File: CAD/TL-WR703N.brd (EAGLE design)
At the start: 47.4 x 50 mm, 241 parts, among them T1 H1601CG, U1 AR9331-AL1A, U2 A3S56F40FTP

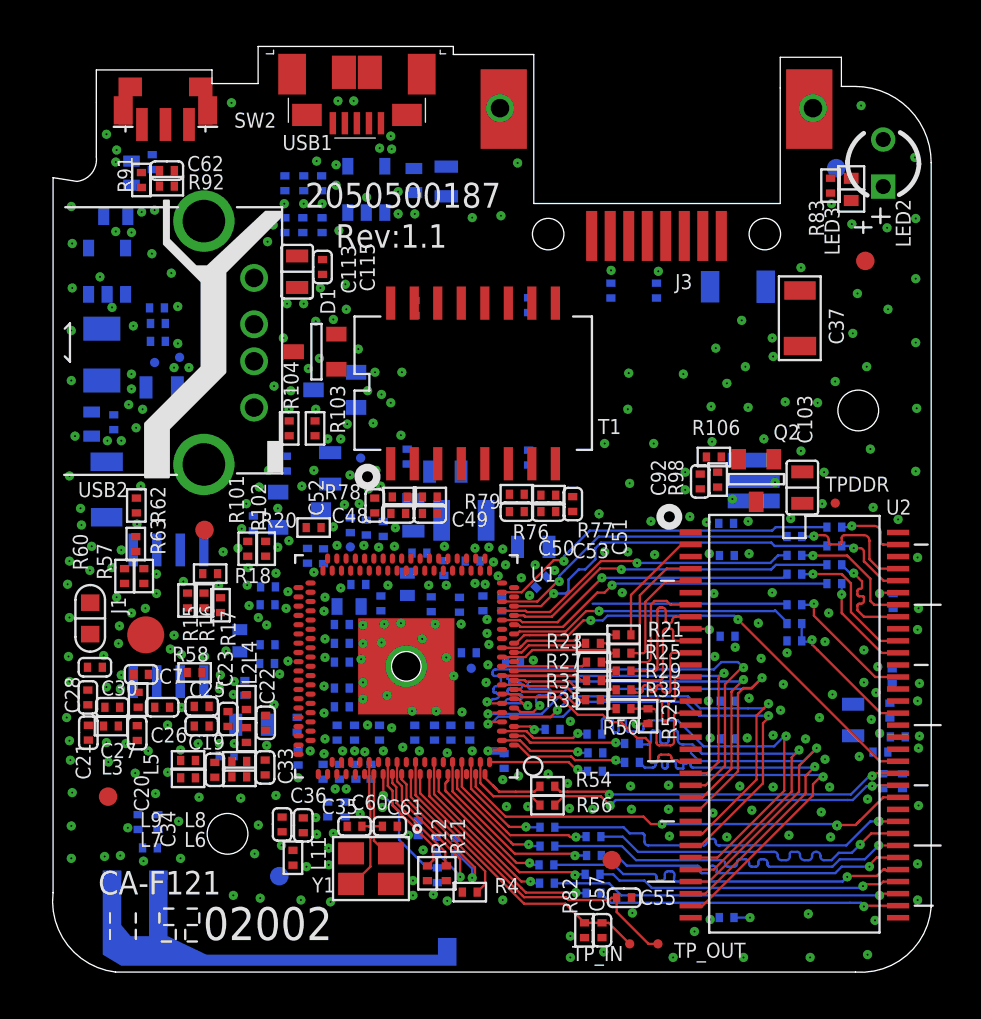
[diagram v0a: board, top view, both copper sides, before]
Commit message: Almost completed traces on top side
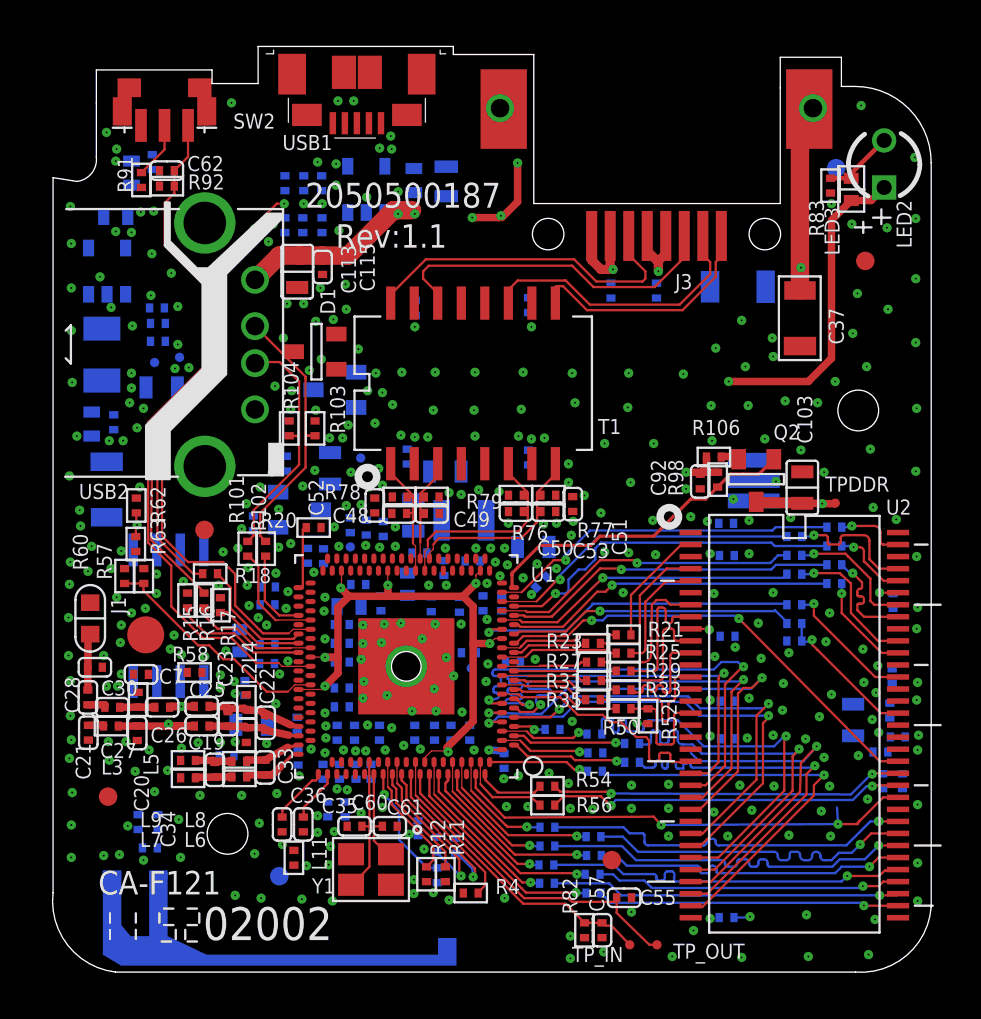
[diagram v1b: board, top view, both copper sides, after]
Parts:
- moved USB2 0.11 mm to (-1.22, 34.4)
- moved C49 0.10 mm to (21.3, 25.3)
- moved R79 0.10 mm to (21.3, 26.2)
- moved R76 0.07 mm to (25.9, 26.3)
- moved LED2 0.07 mm to (45.7, 44.1)
- moved R11 0.07 mm to (22.0, 5.79)
- moved R12 0.07 mm to (21.0, 5.79)
- moved R4 0.07 mm to (23.4, 4.78)
- moved TP_OUT 0.07 mm to (33.5, 1.98)
- moved SW2 0.07 mm to (6.88, 46.2)
- moved C48 0.05 mm to (19.6, 25.3)
- moved C50 0.05 mm to (25.9, 25.4)
- moved TP_IN 0.05 mm to (32.0, 1.98)
- renumbered E$8 to GND
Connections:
- removed net S$41: R37.1, U1.B14
- new net S$102: R101.2, U1.B43
- new net S$103: U1.A58, U1.B13, U1.B21, U1.B31, U1.B36, U1.B47, U1.B69
- new net S$104: D1.3, R102.1, R103.1, USB2.2
- new net S$105: C62.2, R92.2, SW2.3, U1.B48
- new net S$106: R91.2, SW2.2
- new net S$107: SW2.S$1, SW2.S$2
- new net S$108: J3.S$1, USB1.S$1, USB1.S$2, USB1.S$3, USB1.S$4, USB1.S$5, USB1.S$6, USB2.S$1
- new net S$109: R15.2, U1.A54
- new net S$110: R16.2, U1.B46
- new net S$111: R16.1
- new net S$113: R18.1
- new net S$158: C25.1, C26.2
- new net S$168: C19.1, C20.2, L3.2
- new net S$263: U1.B44
- new net S$269: C113.2, C115.2, USB2.1
- new net S$29: J3.8, T1.9
- new net S$290: J3.1, J3.2
- new net S$291: J3.4, J3.5
- new net S$292: C37.2, J3.S$2
- new net S$321: LED2.A, LED3.A
- new net S$329: C92.2, R106.2, R98.2
- new net S$354: C36.2, U1.A68
- new net S$357: C35.2, U1.A69
- new net S$359: C103.1, Q2.3, TPDDR.1
- new net S$365: J3.6, T1.14
- new net S$367: J3.3, T1.16
- new net S$370: C49.1, R79.1, T1.3, U1.A32
- new net S$371: C48.2, R78.2, T1.1, U1.B28
- new net S$372: C52.2, R78.1
- new net S$373: C53.1, R77.1, T1.8, U1.A31
- new net S$374: C50.2, R76.2, T1.6, U1.B27
- new net S$379: Q2.1, R98.1, U1.A20
- new net S$380: Q2.2, R106.1
- new net S$42: J3.7, T1.11
- new net S$420: R37.1, U1.B14
- new net S$452: R62.2, R63.1
- new net S$50: C33.2, L8.1, U1.A64
- new net S$55: LED2.K, LED3.C, R83.2
- new net S$68: C33.1, L6.1, U1.A65
- new net S$70: C34.2, L8.2, L9.1
- new net S$73: C34.1, L6.2, L7.1
- new net S$75: C19.2, C22.1, C23.1, L2.2, U1.A63
- new net S$78: C22.2, C23.2, C25.2, L4.1, U1.A62
- new net S$79: R57.2, R60.2, U1.B50
- new net S$80: C21.2, L3.1
- new net S$81: C27.1, C28.1
- new net S$85: R101.1, R104.1, USB2.3
- new net S$87: C28.2, C30.1, J1.1
- new net S$94: C26.1, C27.2, L5.1
- new net S$95: R20.1, U1.A47
- new net S$96: R17.2, U1.A53
- new net S$97: R18.2, U1.A52
- new net S$98: R102.2, U1.A50
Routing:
- net S$105: track 0.00 -> 38.0 mm
- net S$103: track 0.00 -> 32.6 mm, vias 0 -> 7
- net S$263: track 0.00 -> 30.6 mm
- net S$113: track 0.00 -> 24.4 mm
- net S$111: track 0.00 -> 23.3 mm
- net S$365: track 0.00 -> 18.6 mm
- net S$367: track 0.00 -> 18.2 mm
- net S$420: track 0.00 -> 17.8 mm
- net S$379: track 0.00 -> 17.5 mm
- net S$321: track 0.00 -> 17.1 mm
- net S$104: track 0.00 -> 15.5 mm
- net S$42: track 0.00 -> 15.3 mm
- net S$85: track 0.00 -> 13.7 mm, vias 1 -> 0
- net S$29: track 0.00 -> 13.2 mm
- net S$79: track 0.00 -> 12.9 mm, vias 1 -> 0
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
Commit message: Definitely good progress on top side!
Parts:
- moved LED2 0.11 mm to (45.7, 44.2)
- moved R102 0.11 mm to (12.4, 23.5)
- moved C113 0.11 mm to (14.1, 38.4)
- moved USB1 0.11 mm to (17.2, 48.9)
- moved C48 0.10 mm to (19.6, 25.4)
- moved C49 0.10 mm to (21.3, 25.4)
- moved R101 0.10 mm to (11.4, 23.5)
- moved R17 0.10 mm to (9.91, 20.4)
- moved R52 0.10 mm to (32.9, 14.3)
- moved R63 0.10 mm to (5.33, 23.7)
- moved C52 0.10 mm to (18.2, 25.8)
- moved C92 0.10 mm to (35.8, 27.1)
- moved R15 0.10 mm to (8.13, 20.7)
- moved R16 0.10 mm to (9.02, 20.7)
- moved R20 0.07 mm to (14.9, 24.6)
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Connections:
- net S$452 renamed S$159
- removed net S$321: LED2.A, LED3.A
- removed net S$357: C35.2, U1.A69
- removed net S$367: J3.3, T1.16
- removed net S$370: C49.1, R79.1, T1.3, U1.A32
- removed net S$374: C50.2, R76.2, T1.6, U1.B27
- removed net S$379: Q2.1, R98.1, U1.A20
- removed net S$426: R49.1, U1.B18
- removed net S$49: C61.1, U1.A74, Y1.1
- removed net S$96: R17.2, U1.A53
- removed net VREF: U2.49
- new net $28: R79.2
- new net S$112: U1.A71
- new net S$114: C35.2, U1.A72
- new net S$115: L11.2, U1.A69
- new net S$116: U1.B59
- new net S$117: U1.B60
- new net S$118: U1.B61
- new net S$119: C61.1, U1.B63, Y1.1
- new net S$120: U1.B26
- new net S$121: U1.A19
- new net S$122: U1.B19
- new net S$123: U1.A33
- new net S$130: L9.2
- new net S$132: U1.A38
- new net S$133: U1.B39
- new net S$134: U1.B40
- new net S$135: U1.A49
- new net S$136: U1.A55
- new net S$137: R58.2
- new net S$138: U1.A56
- new net S$139: L4.2
- new net S$141: U1.A61
- new net S$145: U1.A25
- new net S$146: U1.A18
- new net S$147: R16.2, U1.B46
- new net S$148: R101.2, U1.B43
- new net S$150: R15.2, U1.A54
- new net S$151: T1.7
- new net S$152: U1.A48
- new net S$156: C22.2, C23.2, C25.2, L4.1, U1.A62
- new net S$161: D1.2
- new net S$162: J3.7, T1.11
- new net S$163: R83.1
- new net S$164: R91.1
- new net S$165: U1.B49
- new net S$17: L7.2
- new net S$18: U1.A70
- new net S$180: U1.B51
- new net S$186: U1.A57
- new net S$190: R62.1
- new net S$199: R57.1
- new net S$203: U1.B41
- new net S$228: R16.1
- new net S$252: J3.3, T1.16
- new net S$28: C49.1, R79.1, T1.3, U1.A32
- new net S$294: LED2.A, LED3.A
- new net S$331: T1.2
- new net S$409: U1.A30
- new net S$411: U1.A26
- new net S$416: R49.1, U1.B18
- new net S$417: U1.A58, U1.B13, U1.B21, U1.B31, U1.B36, U1.B47, U1.B69
- new net S$430: Q2.1, R98.1, U1.A20
- new net S$431: R29.2, U1.A11
- new net S$44: U2.49
- new net S$449: R17.2, U1.A53
- new net S$69: C51.2, R77.2
- new net S$71: C50.2, R76.2, T1.6, U1.B27
- new net S$84: R46.1, U1.B74
- new net S$86: C57.2, R82.2, TP_IN.1, U1.B68
- new net S$88: R12.2, U1.B65
- new net S$89: C60.2, U1.A73, Y1.3
- net GND: now also C61.2, U1.A74, U1.PAD
- net S$102: now also U1.B42; no longer R101.2, U1.B43
- net S$103: now also U1.B20; no longer U1.A58, U1.B13, U1.B21, U1.B31, U1.B36, U1.B47, U1.B69
- net S$109: now also R15.1; no longer R15.2, U1.A54
- net S$110: now also U1.B45; no longer R16.2, U1.B46
- net S$111: now also R17.1; no longer R16.1
- net S$15: now also U1.B67; no longer C57.2, R82.2, TP_IN.1, U1.B68
- net S$36: now also U1.A12; no longer R29.2, U1.A11
- net S$42: now also T1.10; no longer J3.7, T1.11
- net S$429: no longer U1.A18
- net S$48: now also U1.B62; no longer C60.2, U1.B63, Y1.3
- net S$51: now also U1.B64; no longer R12.2, U1.B65
- net S$67: now also U1.A84; no longer R46.1, U1.B74
- net S$78: now also R58.1; no longer C22.2, C23.2, C25.2, L4.1, U1.A62
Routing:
- net S$417: track 0.00 -> 32.7 mm, vias 1 -> 7
- net S$103: track 32.6 -> 0.76 mm, vias 7 -> 1
- net S$228: track 0.00 -> 23.3 mm
- net S$111: track 23.3 -> 0.67 mm
- net S$426: track 19.3 -> 0.00 mm, vias 1 -> 0
- net S$416: track 0.00 -> 19.3 mm
- net S$367: track 18.2 -> 0.00 mm
- net S$252: track 0.00 -> 18.2 mm, vias 1 -> 0
- net S$430: track 0.00 -> 17.6 mm, vias 1 -> 0
- net S$379: track 17.5 -> 0.00 mm
- net S$294: track 0.00 -> 17.1 mm
- net S$321: track 17.1 -> 0.00 mm, vias 1 -> 0
- net S$86: track 0.00 -> 16.8 mm, vias 1 -> 0
- net S$15: track 16.8 -> 1.16 mm, vias 0 -> 1
- net S$162: track 0.00 -> 15.3 mm
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- added copper zone on layer 1, net GND
- added copper zone on layer 1, net S$166
- added copper zone on layer 1, net S$167
- added copper zone on layer 1, net S$169
- added copper zone on layer 1, net S$170

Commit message: Looks like the top side is done!
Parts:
- moved R91 0.61 mm to (5.04, 43.4)
- moved L5 0.60 mm to (4.86, 15.2)
- moved C28 0.60 mm to (2.14, 15.3)
- moved C30 0.60 mm to (2.52, 17.0)
- moved C62 0.56 mm to (6.46, 43.9)
- moved SW2 0.56 mm to (6.38, 46.3)
- moved R92 0.55 mm to (6.46, 43.0)
- moved C21 0.55 mm to (2.22, 13.4)
- moved C27 0.55 mm to (3.51, 14.8)
- moved C20 0.55 mm to (4.86, 13.4)
- moved GND 0.55 mm to (5.32, 18.7)
- moved J1 0.55 mm to (2.32, 19.6)
- moved R57 0.55 mm to (5.21, 21.9)
- moved R60 0.55 mm to (4.18, 21.9)
- moved R15 0.50 mm to (7.63, 20.6)
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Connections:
- removed net S$141: U1.A61
- removed net S$186: U1.A57
- removed net S$263: U1.B44
- removed net S$352: R39.2, U2.56
- removed net S$365: J3.6, T1.14
- new net S$124: R39.2
- new net S$125: U1.B55
- new net S$127: C34.2, L8.2, L9.1
- new net S$140: U1.A61
- new net S$157: T1.15
- new net S$171: U1.A77
- new net S$172: U2.56
- new net S$178: J1.2
- new net S$182: R101.1, R104.1, USB2.3
- new net S$238: U1.B44
- new net S$41: J3.6, T1.14
- new net S$93: C7.1
- new net S$96: U1.A57
- new net SHIELD: J3.S$1, USB1.S$1, USB1.S$2, USB1.S$3, USB1.S$4, USB1.S$5, USB1.S$6, USB2.S$1
- net GND: now also C103.2, C113.1, C115.1, C20.1, C21.1, C30.2, C36.1, C37.1, C49.2, C51.1, C55.2, C57.1, C62.1, C7.2, C92.1, D1.1, GND.1, L11.1, L5.2, R103.2, R104.2, R20.2, R4.2, R60.1, R92.1, USB1.GND, Y1.2, Y1.4
- net S$108: now also USB1.VBUS; no longer J3.S$1, USB1.S$1, USB1.S$2, USB1.S$3, USB1.S$4, USB1.S$5, USB1.S$6, USB2.S$1
- net S$70: now also L2.1; no longer C34.2, L8.2, L9.1
- net S$76: now also U1.B56; no longer R2.2, U1.A77
- net S$85: now also C48.1, C52.1; no longer R101.1, R104.1, USB2.3
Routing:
- net GND: track 6.00 -> 50.7 mm, vias 289 -> 308
- net S$263: track 30.6 -> 0.00 mm, vias 1 -> 0
- net S$238: track 0.00 -> 24.2 mm
- net SHIELD: track 0.00 -> 20.6 mm
- net S$41: track 0.00 -> 18.8 mm, vias 1 -> 0
- net S$365: track 18.6 -> 0.00 mm
- net S$182: track 0.00 -> 13.9 mm
- net S$85: track 13.6 -> 1.01 mm
- net S$171: track 0.00 -> 8.83 mm, vias 0 -> 1
- net S$76: track 8.69 -> 0.48 mm
- net S$352: track 5.62 -> 0.00 mm, vias 1 -> 0
- net S$108: track 0.00 -> 5.11 mm, vias 0 -> 3
- net S$96: track 0.00 -> 4.96 mm
- net S$172: track 0.00 -> 4.92 mm, vias 0 -> 1
- net S$186: track 4.80 -> 0.00 mm
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- added copper zone on layer 1, net S$107
- added copper zone on layer 1, net S$141
- added copper zone on layer 1, net S$173
- added copper zone on layer 1, net S$175
- added copper zone on layer 1, net S$176
- added copper zone on layer 1, net S$177
- added copper zone on layer 1, net S$179
- added copper zone on layer 1, net S$181
- added copper zone on layer 1, net S$183
- added copper zone on layer 1, net S$184
- added copper zone on layer 1, net S$186
- added copper zone on layer 1, net S$187
- added copper zone on layer 1, net SHIELD
- removed copper zone on layer 1, net S$170
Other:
- board size 47.4 x 50 mm -> 48.3 x 50.1 mm

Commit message: Completed layout reverse engineering!
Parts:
- moved U5 0.73 mm to (3.09, 38.6)
- moved C107 0.62 mm to (4.51, 43.8)
- moved C112 0.62 mm to (3.66, 41.5)
- moved C111 0.59 mm to (3.55, 30.3)
- moved AN1 0.59 mm to (5.96, 5.78)
- moved C108 0.57 mm to (5.68, 44.4)
- moved L14 0.55 mm to (2.96, 34.0)
- moved C106 0.55 mm to (5.99, 34.6)
- moved R99 0.55 mm to (5.99, 35.6)
- moved C110 0.54 mm to (2.41, 30.1)
- moved R110 0.52 mm to (12.9, 41.0)
- moved C18 0.50 mm to (10.7, 15.9)
- moved C24 0.50 mm to (9.75, 12.3)
- moved R100 0.50 mm to (5.99, 36.5)
- moved TP3V3 0.50 mm to (5.86, 33.5)
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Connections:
- removed net S$109: R15.1
- removed net S$111: R17.1
- removed net S$124: R39.2
- removed net S$134: U1.B40
- removed net S$139: L4.2
- removed net S$140: U1.A61
- removed net S$146: U1.A18
- removed net S$151: T1.7
- removed net S$158: C25.1, C26.2
- removed net S$163: R83.1
- removed net S$168: C19.1, C20.2, L3.2
- removed net S$331: T1.2
- removed net S$411: U1.A26
- removed net S$417: U1.A58, U1.B13, U1.B21, U1.B31, U1.B36, U1.B47, U1.B69
- removed net S$48: U1.B62
- removed net S$69: C51.2, R77.2
- removed net S$70: L2.1
- new net S$126: C106.1, R100.2, R99.1, U5.5
- new net S$128: R109.2, R111.2, R112.2, U6.4
- new net S$142: R97.2
- new net S$143: R96.2
- new net S$154: R95.1
- new net S$192: C64.2, C66.2, U1.A84, U1.B1
- new net S$193: C45.2, R64.1, R65.2, R68.2, R71.1
- new net S$194: R107.2, U6.3
- new net S$216: C70.2, Q1.2, R93.2
- new net S$221: D2.2
- new net S$224: C46.1, C47.1, C84.2, Q1.3, T1.2, T1.7, TP2V0.1
- new net S$230: R83.1
- new net S$239: C106.2, C109.2, C110.1, C111.1, L14.1, R99.2, TP3V3.1
- new net S$265: R108.2, R109.1
- new net S$390: R59.1
- new net S$415: C4.2
- new net S$54: C51.2, R76.1, R77.2
- new net S$72: R82.1
- new net S$82: R14.2, R2.1, R3.1
- net GND: now also AN1.GND, C1.2, C100.1, C101.1, C102.1, C104.2, C105.2, C107.1, C108.1, C109.1, C11.1, C110.2, C111.2, C112.2, C114.2, C119.2, C12.1, C13.1, C14.1, C15.2, C16.1, C17.1, C18.2, C2.2, C24.2, C3.2, C31.2, C32.1, C35.1, C4.1, C46.2, C47.2, C5.2, C50.1, C53.2, C60.1, C63.1, C64.1, C65.2, C67.1, C70.1, C71.1, C73.2, C74.1, C75.2, C76.2, C77.1, C78.1, C79.2, C8.2, C80.2, C81.1, C82.1, C83.2, C84.1, C85.1, C86.1, C87.2, C88.2, C89.2, C9.1, C90.2, C91.1, C93.1, C94.1, C95.1, C96.1, C97.2, C98.2, C99.1, D2.1, E$9.GND$1, E$9.GND$2, E$9.GND$3, R100.1, R110.2, R111.1, R13.2, R15.1, R17.1, R53.1, R6.2, R7.2, TPGND.1, U3.4, U5.2, U6.2, USB2.4
- net S$102: now also C86.2
- net S$103: now also C5.1, C87.1, U1.B19
- net S$108: now also C107.2, C108.2, C112.1, C119.1, R113.1, U5.1, U5.4, U6.5
- net S$110: now also USB1.P$1, USB1.P$2; no longer U1.B45
- net S$112: now also L2.1; no longer U1.A71
- net S$116: now also R7.1
- net S$117: now also C88.1, C89.1, C90.1, R96.1, U1.B61, U1.B62
- net S$118: now also L14.2, U5.3; no longer U1.B61
- net S$120: now also C67.2, C71.2, C73.1, C74.2, C75.1, C76.1, C77.2, C78.2, C83.1, R94.2, TP1V2.1, U1.A26, U1.A58, U1.B13, U1.B21, U1.B31, U1.B36, U1.B47, U1.B69
- net S$121: now also C63.2
- net S$122: now also C81.2, U1.B45; no longer U1.B19
- net S$125: now also C91.2, R97.1
- net S$130: now also C25.1, C26.2
- net S$132: now also C101.2, C94.2, C95.2, TP2V5.1
- net S$133: now also C102.2, C96.2
- net S$135: now also C97.1
- net S$136: now also C98.1, R84.1
- net S$137: now also U3.7
- net S$138: now also R84.2
- net S$145: now also L13.2
- net S$15: now also C100.2, C99.2
- net S$152: now also C2.1
- net S$157: now also R64.2
- net S$159: now also U3.3
- net S$165: now also U3.1
- net S$17: now also C19.1, C20.2, L3.2
- net S$172: now also R39.2
- net S$178: now also C29.1, C31.1
- net S$18: now also C104.1, C105.1, C3.1, C38.1, C79.1, C80.1, C82.2, L1.2, L13.1, R94.1, U1.A61, U1.A71, U1.B40
- net S$180: now also U3.6
- net S$182: now also D2.3
- net S$199: now also U3.2
- net S$203: now also Q1.1, R93.1
- net S$228: now also R107.1, R108.1, R110.1
- net S$269: now also R113.2, U6.1
- net S$290: now also R65.1
- net S$291: now also R68.1
- net S$292: now also C45.1
- net S$36: now also C65.1
- net S$409: now also C93.2
- net S$42: now also R71.2
- net S$429: now also U1.A18
- net S$44: now also C16.2, C17.2, R59.2, R6.1
- net S$51: now also R14.1
- net S$53: now also C6.2, R55.2
- net S$60: now also C6.1, R55.1
- net S$67: now also C18.1, C24.1, C85.2, L4.2; no longer U1.A84
- net S$76: now also C1.1, L1.1
- net S$78: now also R95.2
- net S$83: now also AN1.RF, C29.2, C32.2; no longer C66.2, U1.B1
- net S$93: now also U3.8
- net S$96: now also U3.5
- net SHIELD: now also C114.1, USB2.S$2
- net VDD: now also C13.2, C14.2
- net VDDQ: now also C11.2, C12.2, C15.1, C8.1, C9.2
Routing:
- net S$120: track 0.72 -> 48.1 mm, vias 1 -> 11
- net S$18: track 0.79 -> 38.9 mm, vias 1 -> 4
- net S$230: track 0.00 -> 33.9 mm, vias 1 -> 2
- net S$417: track 32.3 -> 0.00 mm, vias 7 -> 0
- net SHIELD: track 20.6 -> 39.6 mm
- net S$224: track 0.00 -> 18.0 mm, vias 1 -> 4
- net S$193: track 0.00 -> 17.5 mm
- net S$178: track 1.76 -> 17.7 mm
- net GND: track 50.7 -> 35.8 mm, vias 308 -> 321
- net S$54: track 0.00 -> 7.29 mm, vias 1 -> 2
- net S$17: track 0.85 -> 7.73 mm, vias 1 -> 2
- net S$126: track 0.00 -> 6.26 mm, vias 1 -> 0
- net S$3: track 18.1 -> 23.0 mm
- net S$289: track 4.86 -> 0.00 mm, vias 3 -> 0
- net S$192: track 0.00 -> 4.73 mm, vias 0 -> 2
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- added copper zone on layer 16, net GND
- added copper zone on layer 1, net S$108
- added copper zone on layer 16, net S$108
- added copper zone on layer 16, net S$109
- added copper zone on layer 16, net S$111
- added copper zone on layer 16, net S$117
- added copper zone on layer 16, net S$118
- added copper zone on layer 16, net S$124
- added copper zone on layer 16, net S$129
- added copper zone on layer 16, net S$134
- added copper zone on layer 1, net S$139
- added copper zone on layer 1, net S$140
- added copper zone on layer 16, net S$146
- added copper zone on layer 1, net S$151
- added copper zone on layer 1, net S$153
- added copper zone on layer 16, net S$155
- added copper zone on layer 16, net S$158
- added copper zone on layer 16, net S$163
- added copper zone on layer 16, net S$168
- added copper zone on layer 1, net S$170
- added copper zone on layer 16, net S$174
- added copper zone on layer 16, net S$18
- added copper zone on layer 1, net S$185
- added copper zone on layer 1, net S$188
- added copper zone on layer 1, net S$191
- added copper zone on layer 16, net S$195
- added copper zone on layer 16, net S$196
- added copper zone on layer 16, net S$197
- added copper zone on layer 1, net S$198
- added copper zone on layer 1, net S$200
- added copper zone on layer 16, net S$201
- added copper zone on layer 16, net S$239
- added copper zone on layer 16, net S$269
- added copper zone on layer 16, net S$48
- added copper zone on layer 16, net S$69
- added copper zone on layer 16, net S$70
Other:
- board size 48.3 x 50.1 mm -> 48.5 x 50.1 mm
